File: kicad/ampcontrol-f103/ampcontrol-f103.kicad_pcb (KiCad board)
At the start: 2 copper layers, 89.3 x 55 mm, 71 parts, among them J1 SP, J10 Buttons, J11 Encoder, J12 LCD_CTRL, J13 I2C, J14 I2C, J15 I2C, J16 SPI_2.4, J17 SPI_2.8, J18 SPI_3.2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

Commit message: Add GND to external SPI sockets
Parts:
- J17, J18: footprint Connector_PinSocket_2.54mm:PinSocket_1x04_P2.54mm_Vertical -> Connector_PinSocket_2.54mm:PinSocket_1x05_P2.54mm_Vertical
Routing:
- net GNDD: track 608.9 -> 619.2 mm
- net /SD_MOSI: track 127.7 -> 126.9 mm

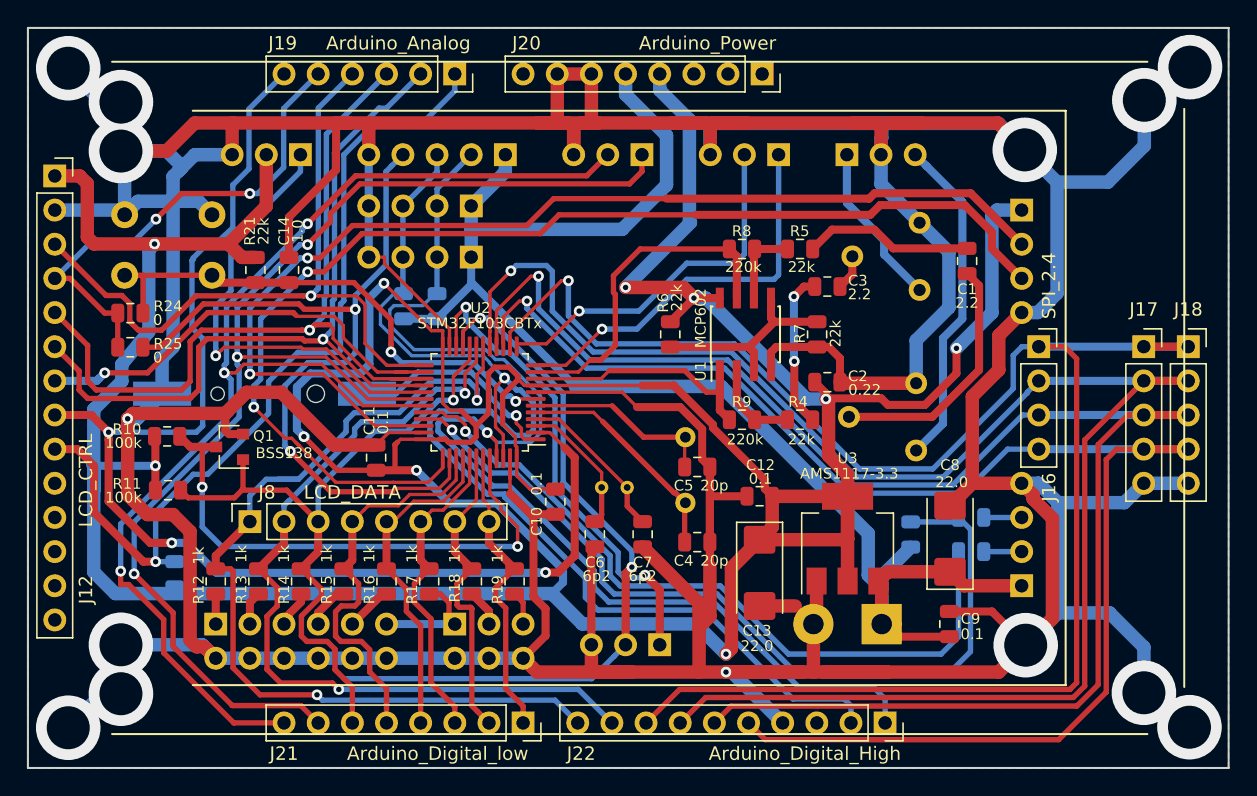
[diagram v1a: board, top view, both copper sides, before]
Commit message: Move ampcontrol-f103 to Kicad 6
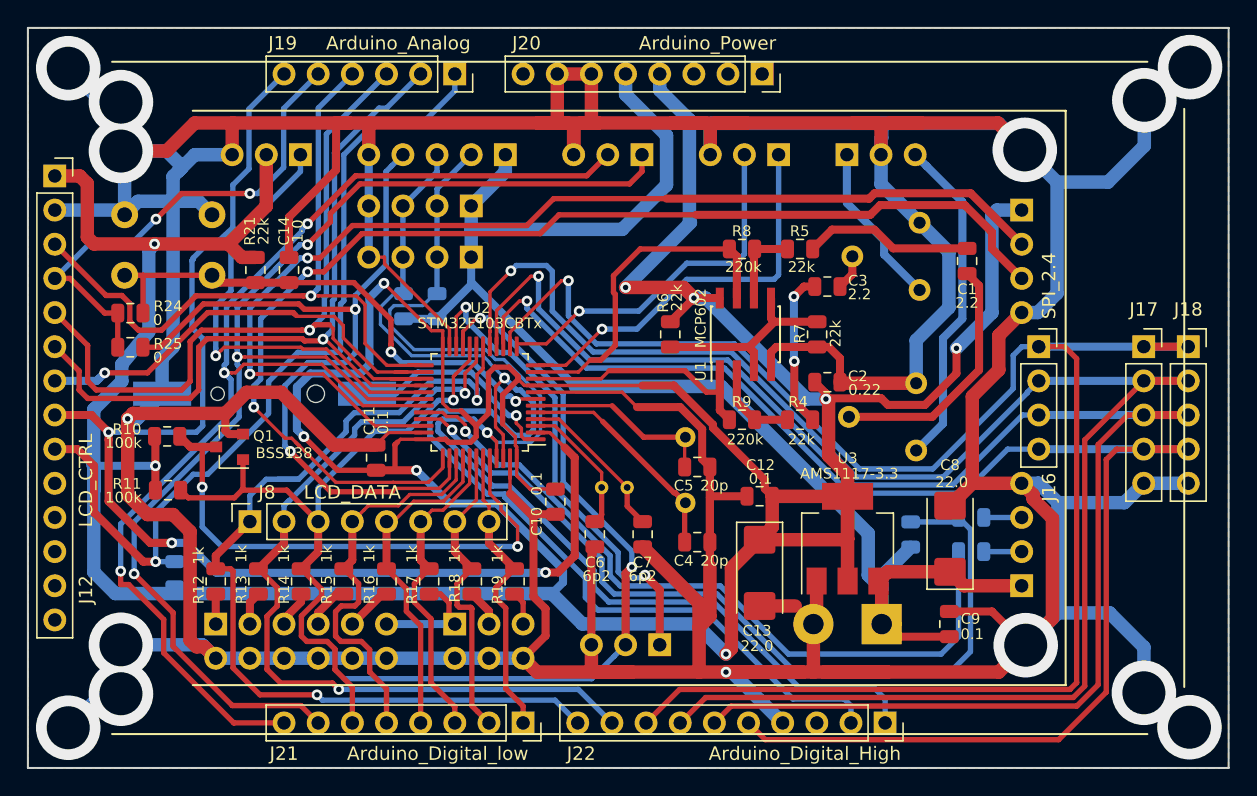
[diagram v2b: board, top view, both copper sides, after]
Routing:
- net GNDD: track 619.2 -> 616.3 mm
- net +3V3: track 350.4 -> 347.6 mm
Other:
- net class Default removed
- net class Power removed

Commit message: Swap MUTE and STBY in schematic, with no PCB change
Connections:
- J12 pad 10: Net-(J12-Pad10) -> unconnected-(J12-Pad10)
- J12 pad 11: Net-(J12-Pad11) -> unconnected-(J12-Pad11)
- J12 pad 12: Net-(J12-Pad12) -> unconnected-(J12-Pad12)
- J12 pad 13: Net-(J12-Pad13) -> unconnected-(J12-Pad13)
- J12 pad 14: Net-(J12-Pad14) -> unconnected-(J12-Pad14)
- J20 pad 1: Net-(J20-Pad1) -> unconnected-(J20-Pad1)
- J20 pad 2: Net-(J20-Pad2) -> unconnected-(J20-Pad2)
- J20 pad 3: Net-(J20-Pad3) -> unconnected-(J20-Pad3)
- J20 pad 8: Net-(J20-Pad8) -> unconnected-(J20-Pad8)
- J22 pad 3: Net-(J22-Pad3) -> unconnected-(J22-Pad3)
- J6 pad 1: /STBY -> /MUTE
- J6 pad 2: /MUTE -> /STBY
- U2 pad 21: /MUTE -> /STBY
- U2 pad 22: /STBY -> /MUTE
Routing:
- net /STBY: track 35.8 -> 55.5 mm
- net /MUTE: track 55.5 -> 35.8 mm
